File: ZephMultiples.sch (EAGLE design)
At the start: 23 parts

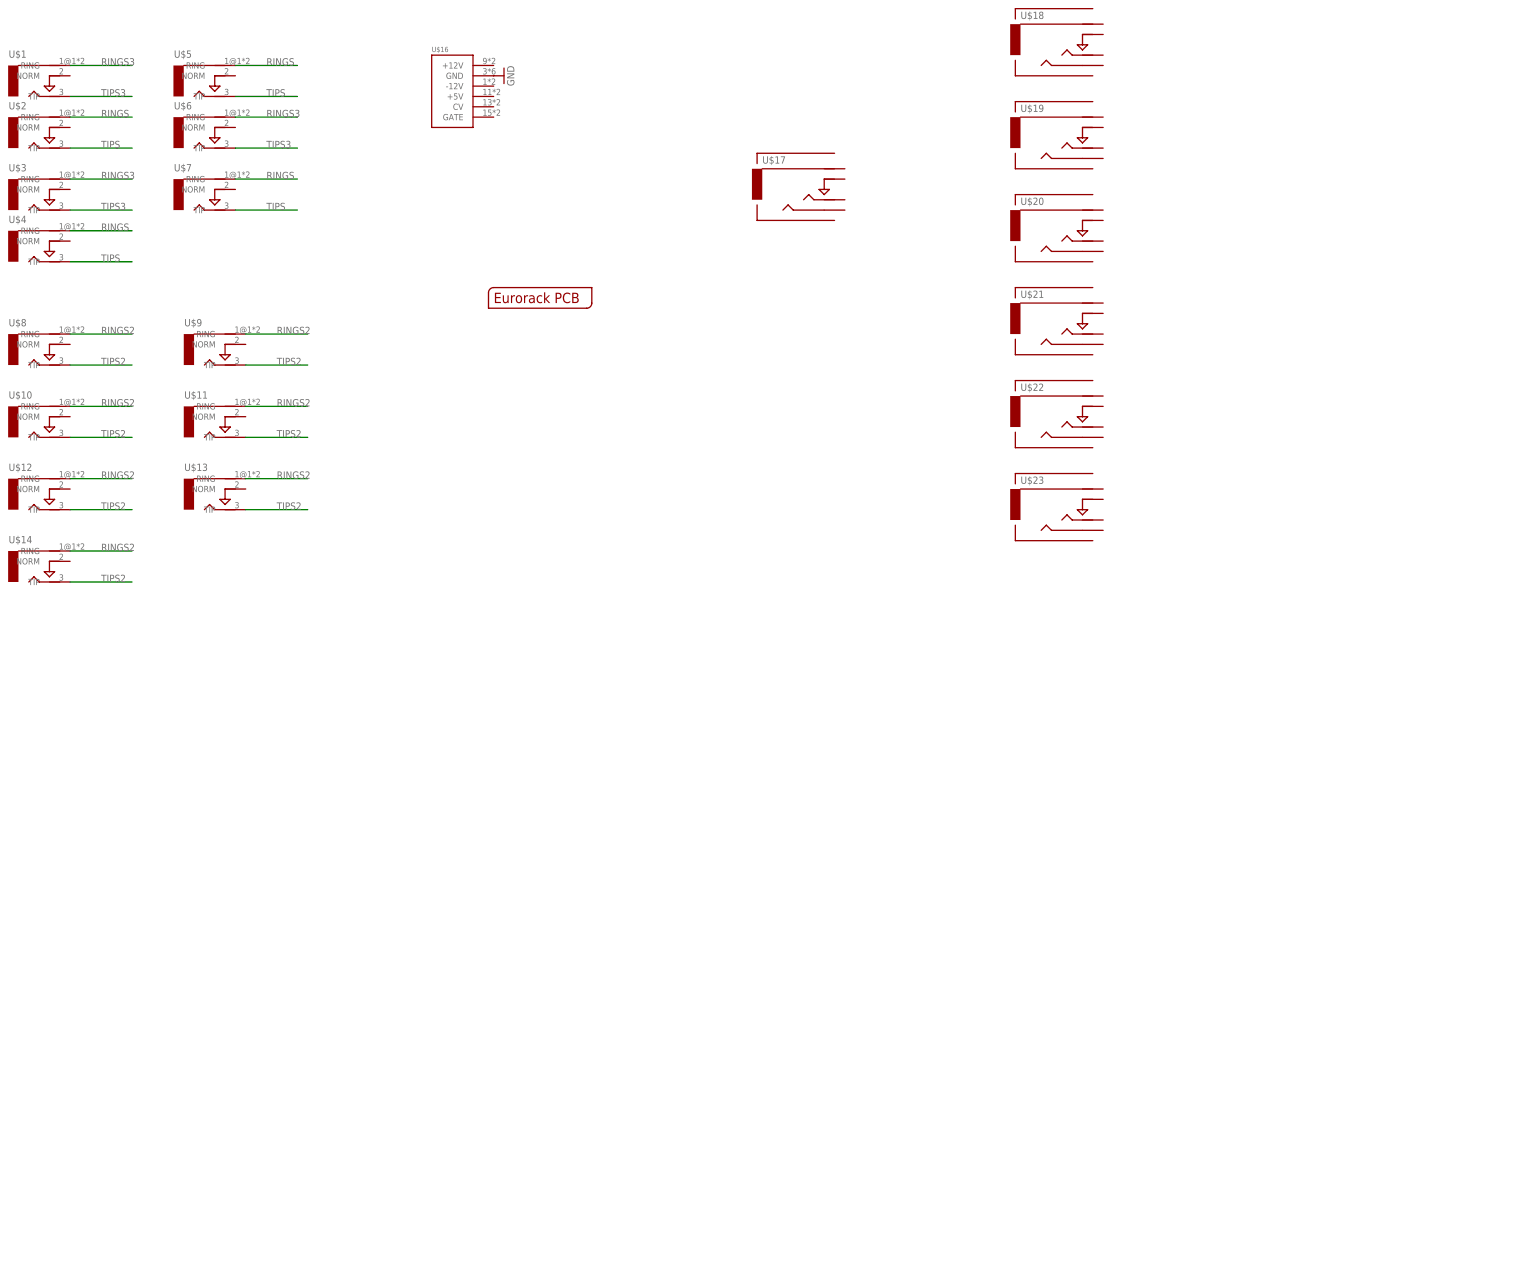
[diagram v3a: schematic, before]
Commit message: Buffered Multipes Spacepacked
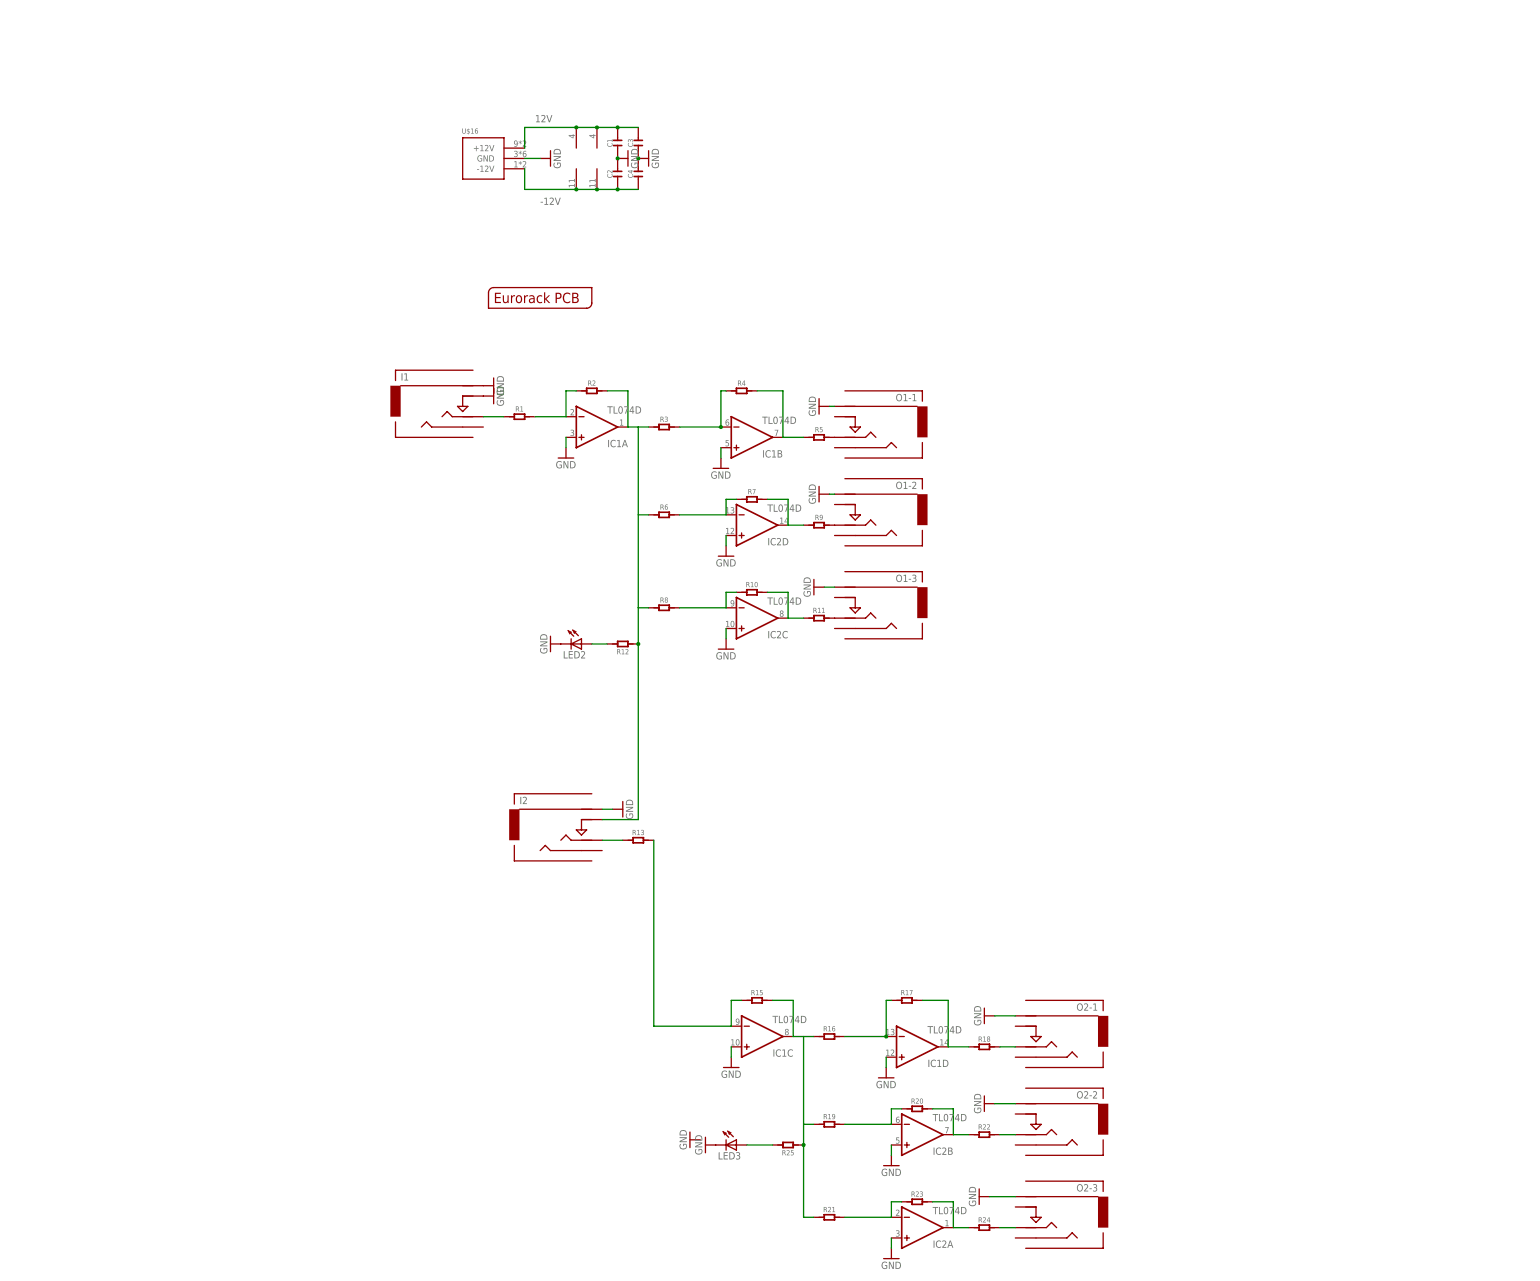
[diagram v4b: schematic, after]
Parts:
- removed U$1, U$10, U$11, U$12, U$13, U$14, U$2, U$3, U$4, U$5, U$6, U$7, U$8, U$9: AUDIO-JACKERTHENVAR, erthenvar:AUDIO-JACKERTHENVAR
- removed U$17: AUDIO-JACKINPUT, EurorackModularParts:AUDIO-JACKINPUT
- removed U$18, U$19, U$20, U$21, U$22, U$23: AUDIO-JACKOUTPUT, EurorackModularParts:AUDIO-JACKOUTPUT
- added C1, C2, C3, C4: (no value), OPL:C-0603
- added I1: In 1, EurorackModularParts:AUDIO-JACKINPUT
- added I2: In 2, EurorackModularParts:AUDIO-JACKINPUT
- added IC1, IC2: TL074D, EurorackModularParts:TL074D
- added LED2, LED3: (no value), SparkFun-LED:LED3MM
- added O1-1, O1-2, O1-3, O2-1, O2-2, O2-3: AUDIO-JACKOUTPUT, EurorackModularParts:AUDIO-JACKOUTPUT
- added R1, R10, R11, R12, R13, R15, R16, R17, R18, R19, R2, R20, R21, R22, R23, R24, R25, R3, R4, R5, R6, R7, R8, R9: (no value), OPL:R-0603
- U$15: value EURORACK_PCB8HP -> EURORACK_PCB4HP; device EurorackModularParts:EURORACK_PCB8HP -> EurorackModularParts:EURORACK_PCB4HP
- U$16: value POWER -> POWER_SIMPLE10; device EurorackModularParts:POWER -> EurorackModularParts:POWER_SIMPLE10
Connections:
- removed net RINGS: U$2.RING, U$4.RING, U$5.RING, U$7.RING
- removed net RINGS2: U$10.RING, U$11.RING, U$12.RING, U$13.RING, U$14.RING, U$8.RING, U$9.RING
- removed net RINGS3: U$1.RING, U$3.RING, U$6.RING
- removed net TIPS: U$2.TIP, U$4.TIP, U$5.TIP, U$7.TIP
- removed net TIPS2: U$10.TIP, U$11.TIP, U$12.TIP, U$13.TIP, U$14.TIP, U$8.TIP, U$9.TIP
- removed net TIPS3: U$1.TIP, U$3.TIP, U$6.TIP
- new net -12V: C2.1, C4.1, IC1P.V-, IC2P.V-, U$16.-12V
- new net 12V: C1.2, C3.2, IC1P.V+, IC2P.V+, U$16.+12V
- new net N$1: I1.TIP, R1.1
- new net N$10: LED2.A, R12.2
- new net N$11: O1-1.TIP, R5.2
- new net N$12: O1-2.TIP, R9.2
- new net N$13: O1-3.TIP, R11.2
- new net N$14: I2.TIP, R13.1
- new net N$15: IC1C.-IN, R13.2, R15.1
- new net N$16: IC1C.OUT, R15.2, R16.1, R19.1, R21.1, R25.1
- new net N$17: IC1D.-IN, R16.2, R17.1
- new net N$18: IC1D.OUT, R17.2, R18.1
- new net N$19: IC2B.-IN, R19.2, R20.1
- new net N$2: IC1A.-IN, R1.2, R2.1
- new net N$20: IC2A.-IN, R21.2, R23.1
- new net N$21: IC2B.OUT, R20.2, R22.1
- new net N$22: IC2A.OUT, R23.2, R24.1
- new net N$23: LED3.A, R25.2
- new net N$24: O2-1.TIP, R18.2
- new net N$25: O2-2.TIP, R22.2
- new net N$26: O2-3.TIP, R24.2
- new net N$3: I2.SWITCH, IC1A.OUT, R12.1, R2.2, R3.1, R6.1, R8.1
- new net N$4: IC1B.-IN, R3.2, R4.1
- new net N$5: IC1B.OUT, R4.2, R5.1
- new net N$6: IC2D.-IN, R6.2, R7.1
- new net N$7: IC2C.-IN, R10.1, R8.2
- new net N$8: IC2D.OUT, R7.2, R9.1
- new net N$9: IC2C.OUT, R10.2, R11.1
- net GND: now also C1.1, C2.2, C3.1, C4.2, I1.RING, I1.SWITCH, I2.RING, IC1A.+IN, IC1B.+IN, IC1C.+IN, IC1D.+IN, IC2A.+IN, IC2B.+IN, IC2C.+IN, IC2D.+IN, LED2.C, LED3.C, O1-1.RING, O1-2.RING, O1-3.RING, O2-1.RING, O2-2.RING, O2-3.RING

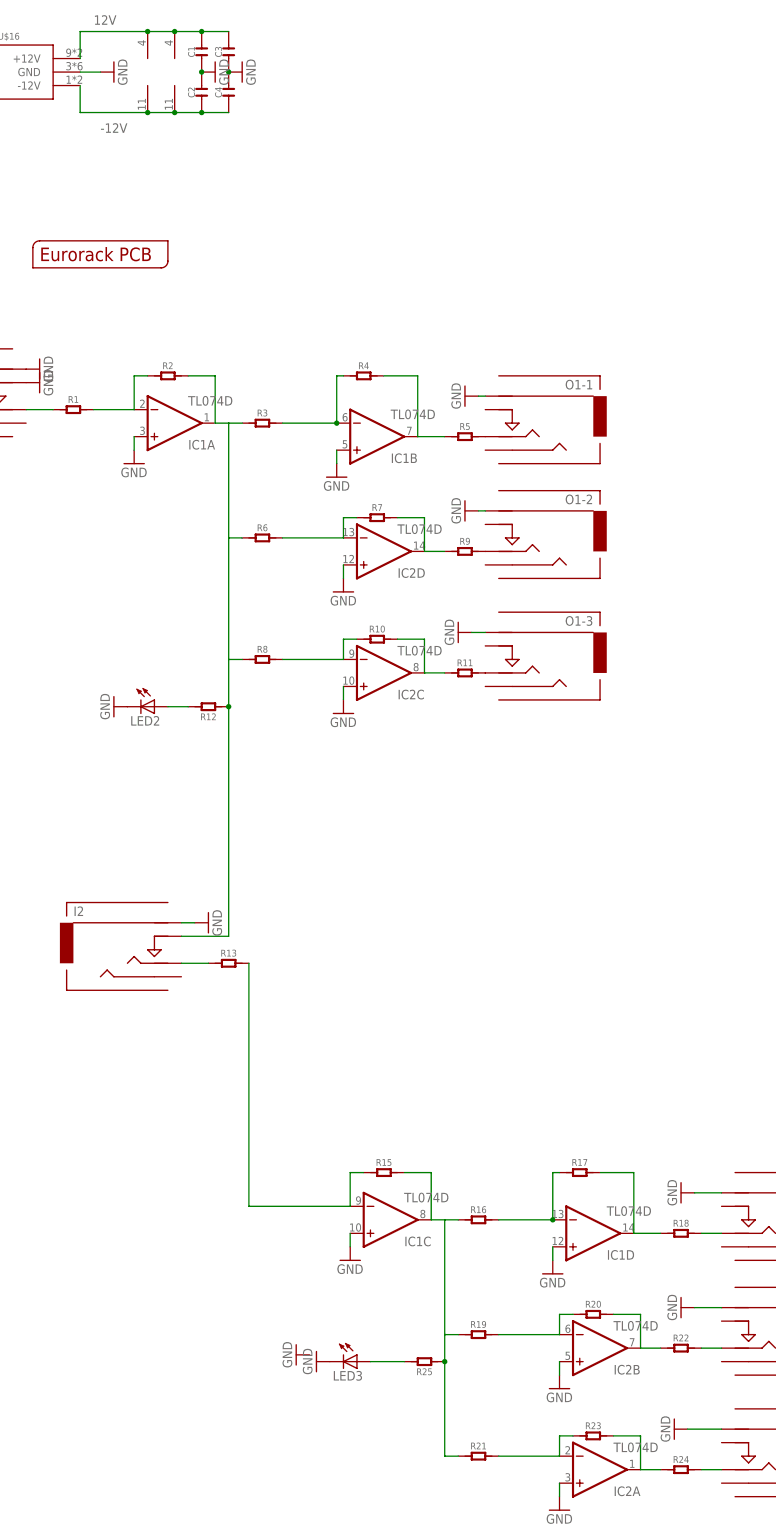
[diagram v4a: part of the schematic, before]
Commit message: Added inverted silk for 10pin power - added opamps for leds
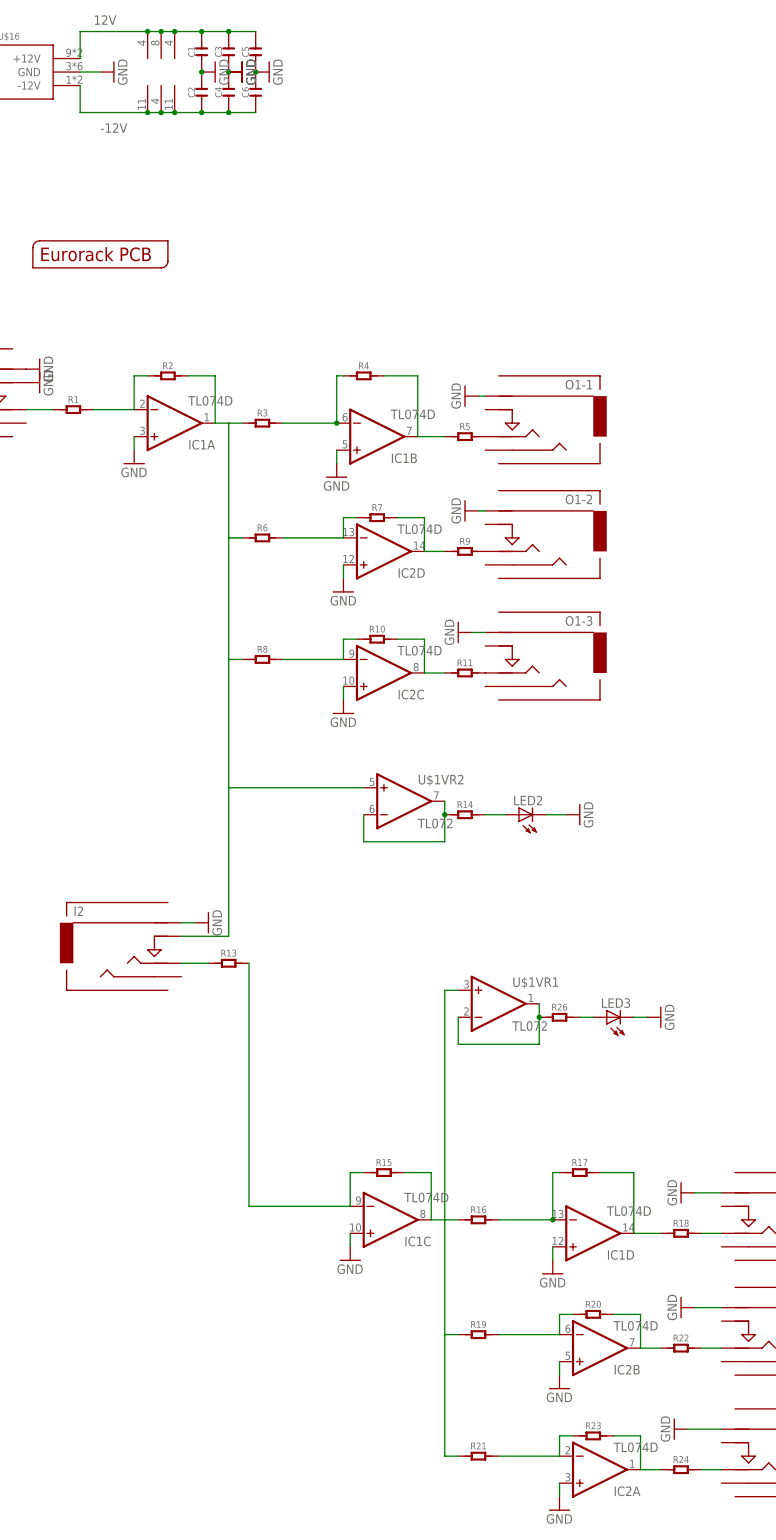
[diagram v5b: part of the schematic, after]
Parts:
- removed R12, R25: (no value), OPL:R-0603
- added C5, C6: (no value), OPL:C-0603
- added R14, R26: (no value), OPL:R-0603
- added U$1: TL072, EurorackModularParts:TL072
- U$16: value POWER_SIMPLE10 -> POWER_SIMPLE10-OTHERSIDE; device EurorackModularParts:POWER_SIMPLE10 -> EurorackModularParts:POWER_SIMPLE10-OTHERSIDE
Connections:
- removed net N$10: LED2.A, R12.2
- removed net N$23: LED3.A, R25.2
- new net N$27: R14.1, U$1VR2.-IN, U$1VR2.OUT
- new net N$28: R26.1, U$1VR1.-IN, U$1VR1.OUT
- new net N$29: LED2.A, R14.2
- new net N$30: LED3.A, R26.2
- net -12V: now also C6.1, U$1VR3.V-
- net 12V: now also C5.2, U$1VR3.V+
- net GND: now also C5.1, C6.2
- net N$16: now also U$1VR1.+IN; no longer R25.1
- net N$3: now also U$1VR2.+IN; no longer R12.1
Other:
- moved on the sheet: LED2, LED3
